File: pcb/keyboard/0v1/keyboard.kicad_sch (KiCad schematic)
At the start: 14 parts, among them U1 113990583, Y1 32.768

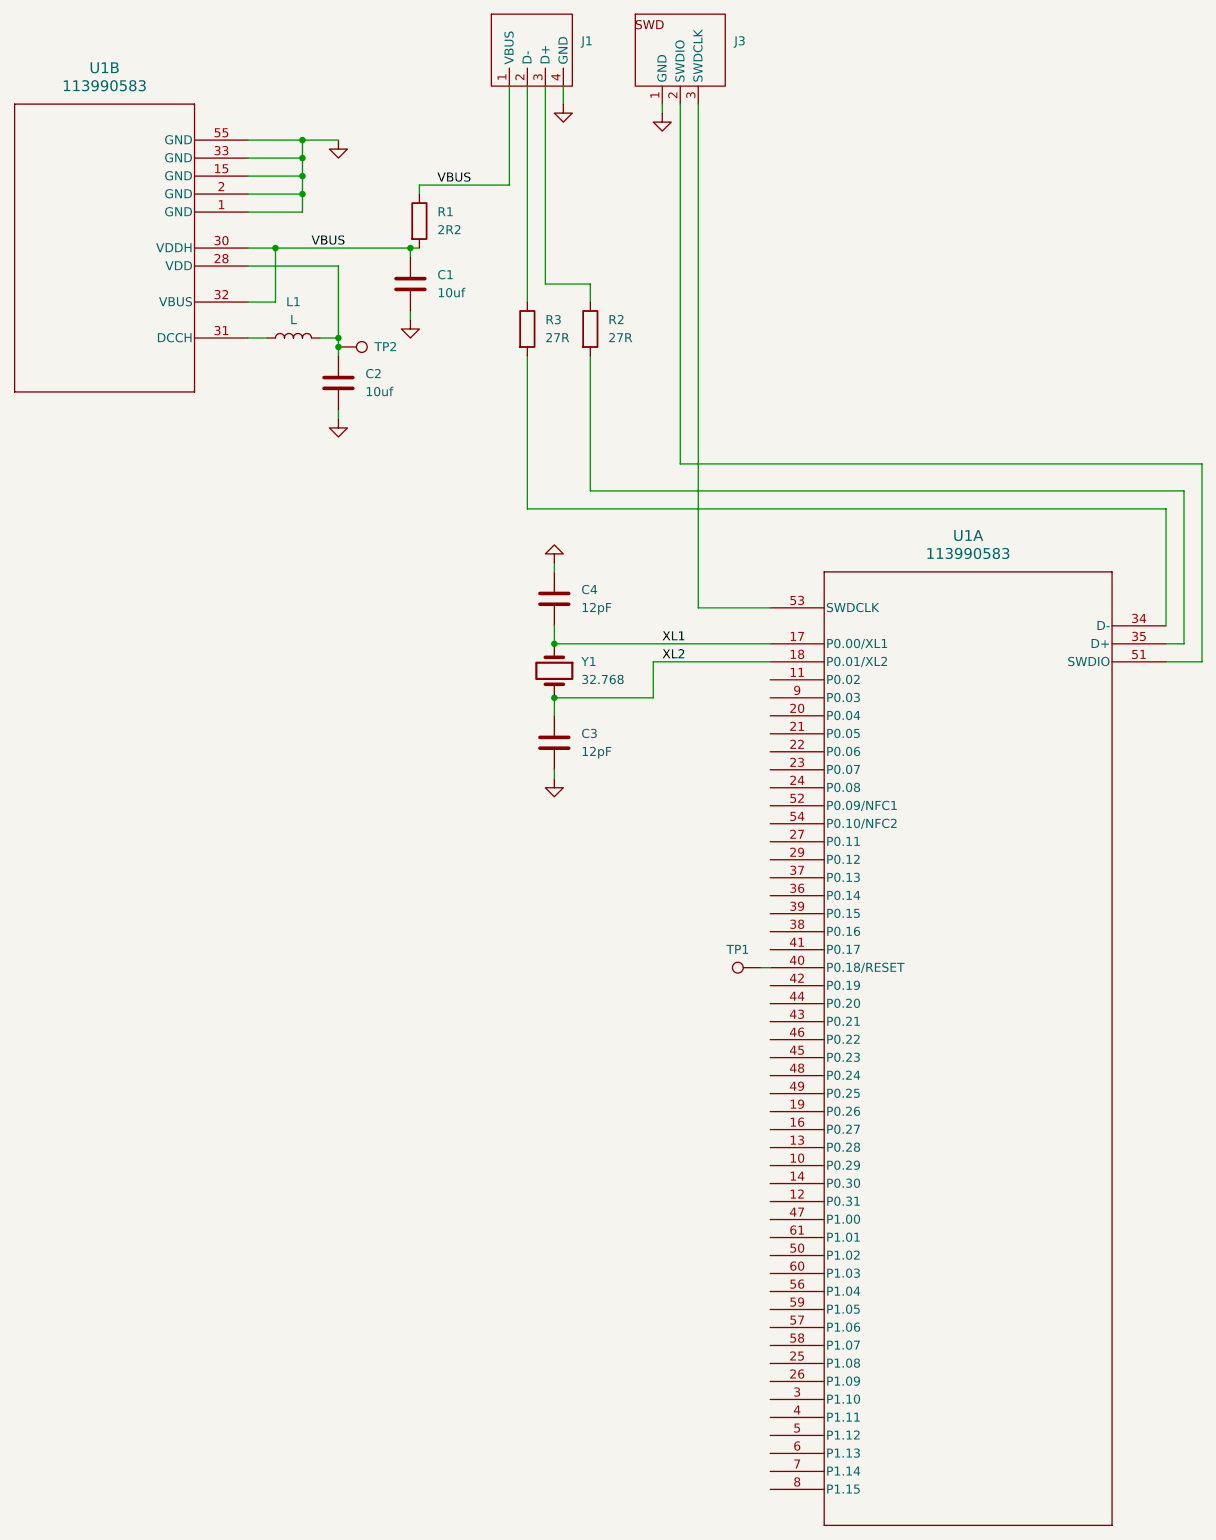
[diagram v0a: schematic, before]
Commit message: Re-created the non-open source symbols for the NRF module
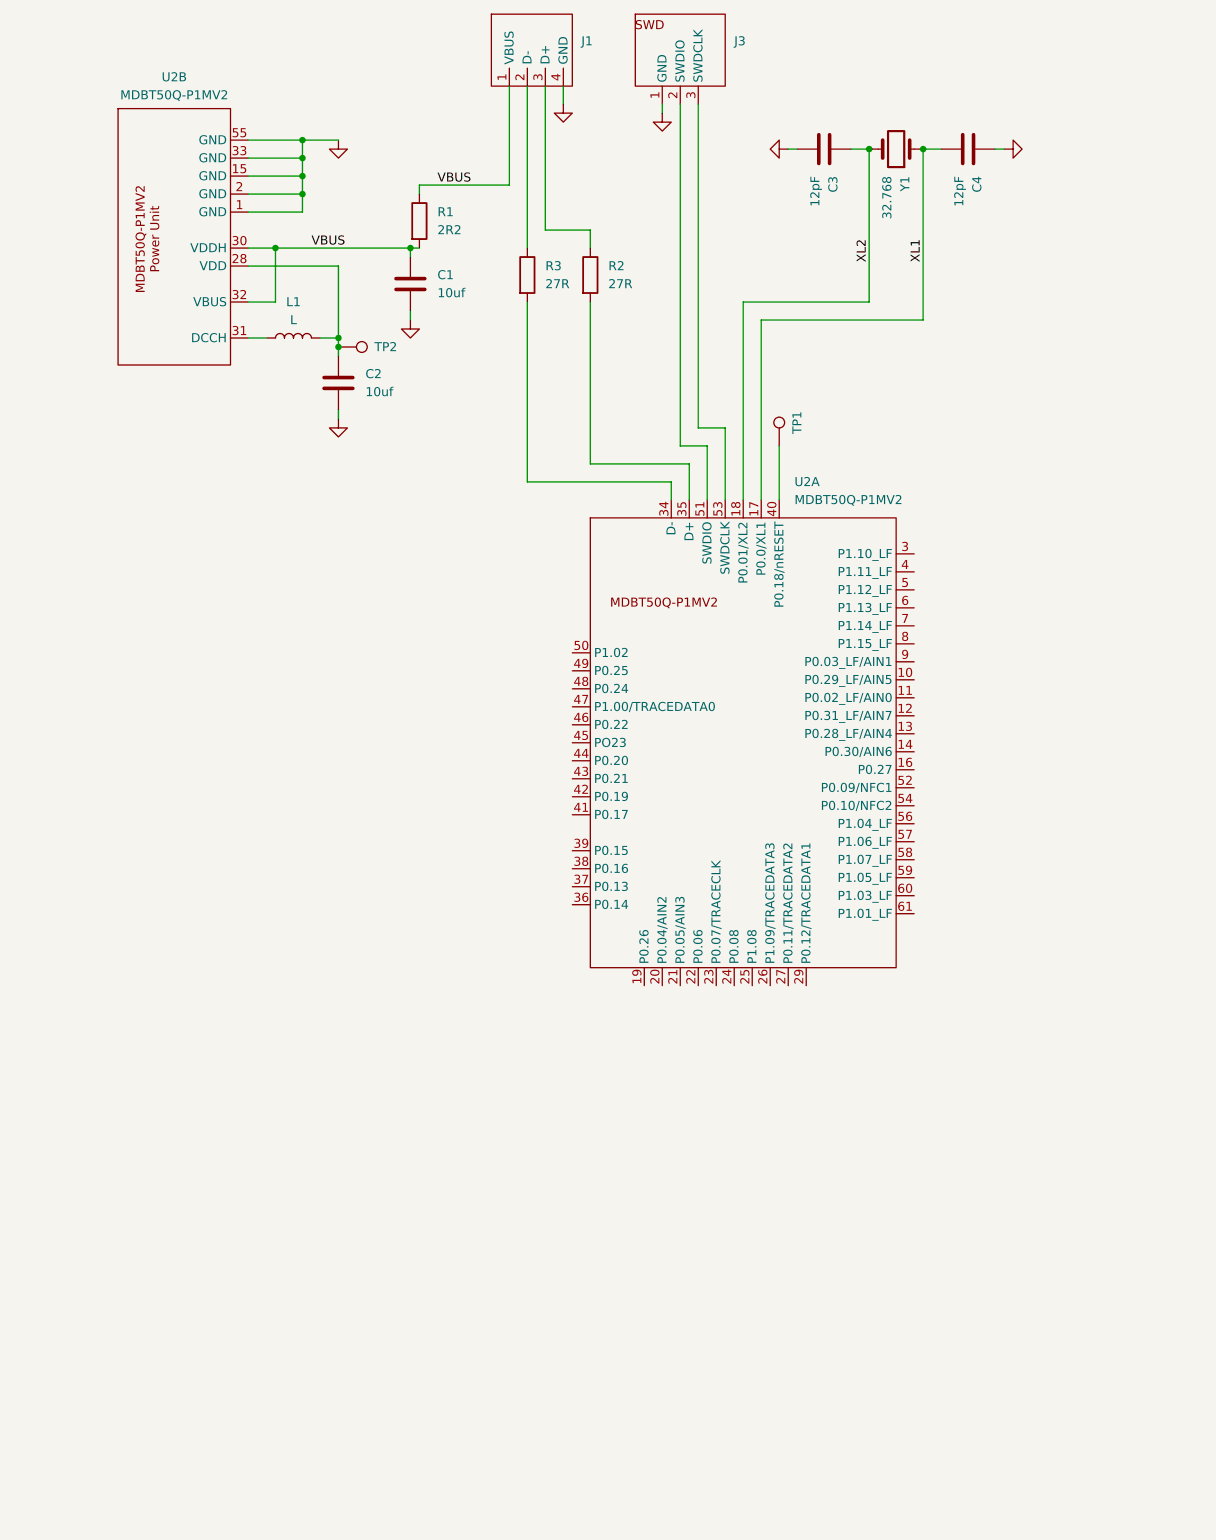
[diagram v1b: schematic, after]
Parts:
- removed U1: 113990583, 113990583_SEE, symbol MDBT50Q-1MV2 & MDBT50Q-P1MV2:113990583
- added U2: MDBT50Q-P1MV2, symbol TH-A10C:MDBT50Q-P1MV2
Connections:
- net GND: now also U2.1 (GND), U2.15 (GND), U2.2 (GND), U2.33 (GND), U2.55 (GND)
- net VBUS: now also U2.30 (VDDH), U2.32 (VBUS)
- net XL1: now also U2.17 (P0.0/XL1)
- net XL2: now also U2.18 (P0.01/XL2)
- net at C2.1, L1.2, TP2.1: now also U2.28 (VDD)
- net at L1.1: now also U2.31 (DCCH)
- net at R2.2: now also U2.35 (D+)
- net at R3.2: now also U2.34 (D-)
- net at TP1.1: now also U2.40 (P0.18/nRESET)
- net at J3.2 (SWDIO): now also U2.51 (SWDIO)
- net at J3.3 (SWDCLK): now also U2.53 (SWDCLK)
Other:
- moved on the sheet: C3, C4, R2, R3, TP1, Y1
